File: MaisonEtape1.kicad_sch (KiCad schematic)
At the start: 6 parts, among them SW1 SW_DIP_x01, SW2 SW_DIP_x01, SW3 SW_DIP_x01, U1 ATmega328-P, U2 ATmega328-P

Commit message: Photon
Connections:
- net GND: now also Lt.22 (GND), Lt.8 (GND), U1.22 (GND), U1.8 (GND), U2.22 (GND), U2.8 (GND)
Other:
- added sheet Photon (Photon.kicad_sch)
- note added: "F1"
- note added: "F2"
- note added: "MASTER"
- note added: "Porte"
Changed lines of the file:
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@@
+    (stroke (width 0) (type default))
+  )
+  (wire (pts (xy 201.93 146.05) (xy 201.93 152.4))
     (stroke (width 0) (type default))
   )
@@
     (stroke (width 0) (type default))
   )
+  (wire (pts (xy 134.62 146.05) (xy 134.62 152.4))
+    (stroke (width 0) (type default))
+  )
   (wire (pts (xy 217.17 85.09) (xy 224.79 85.09))
     (stroke (width 0) (type default))
@@
   (wire (pts (xy 102.87 125.73) (xy 105.41 125.73))
     (stroke (width 0) (type default))
+  )
+  (wire (pts (xy 87.63 146.05) (xy 87.63 152.4))
+    (stroke (width 0) (type default))
+  )
+  (text "F2\n" (at 95.25 50.8 0)
+    (effects (font (size 2 2)) (justify left bottom))
+  )
+  (text "F1" (at 87.63 30.48 0)
+    (effects (font (size 2 2)) (justify left bottom))
+  )
+  (text "Porte" (at 130.81 30.48 0)
+    (effects (font (size 2 2)) (justify left bottom))
+  )
+  (text "MASTER" (at 204.47 147.32 0)
+    (effects (font (size 2 2)) (justify left bottom))
   )
   (global_label "i2c_SCL" (shape input) (at 110.49 113.03 0) (fields_autoplaced)
@@
     )
   )
+  (symbol (lib_id "power:GND") (at 134.62 152.4 0) (unit 1)
+    (in_bom yes) (on_board yes) (dnp no) (fields_autoplaced)
+    (property "Reference" "#PWR016" (at 134.62 158.75 0)
+      (effects (font (size 1.27 1.27)) hide)
+    )
+    (property "Value" "GND" (at 134.62 157.48 0)
+      (effects (font (size 1.27 1.27)))
+    )
+    (property "Footprint" "" (at 134.62 152.4 0)
+      (effects (font (size 1.27 1.27)) hide)
+    )
+    (property "Datasheet" "" (at 134.62 152.4 0)
+      (effects (font (size 1.27 1.27)) hide)
+    )
+    (pin "1")
+    (instances
+      (project "MaisonEtape1"
+        (path "/ed06f8de-d1bb-4b1a-bfe3-5df11d3a9162"
+          (reference "#PWR016") (unit 1)
+        )
+      )
+    )
+  )
+  (symbol (lib_id "power:GND") (at 87.63 152.4 0) (unit 1)
+    (in_bom yes) (on_board yes) (dnp no) (fields_autoplaced)
+    (property "Reference" "#PWR015" (at 87.63 158.75 0)
+      (effects (font (size 1.27 1.27)) hide)
+    )
+    (property "Value" "GND" (at 87.63 157.48 0)
+      (effects (font (size 1.27 1.27)))
+    )
+    (property "Footprint" "" (at 87.63 152.4 0)
+      (effects (font (size 1.27 1.27)) hide)
+    )
+    (property "Datasheet" "" (at 87.63 152.4 0)
+      (effects (font (size 1.27 1.27)) hide)
+    )
+    (pin "1")
+    (instances
+      (project "MaisonEtape1"
+        (path "/ed06f8de-d1bb-4b1a-bfe3-5df11d3a9162"
+          (reference "#PWR015") (unit 1)
+        )
+      )
+    )
+  )
   (symbol (lib_id "Switch:SW_DIP_x01") (at 133.35 39.37 0) (unit 1)
     (in_bom yes) (on_board yes) (dnp no) (fields_autoplaced)
@@
         (path "/ed06f8de-d1bb-4b1a-bfe3-5df11d3a9162"
           (reference "#PWR06") (unit 1)
+        )
+      )
+    )
+  )
+  (symbol (lib_id "power:GND") (at 201.93 152.4 0) (unit 1)
+    (in_bom yes) (on_board yes) (dnp no) (fields_autoplaced)
+    (property "Reference" "#PWR017" (at 201.93 158.75 0)
+      (effects (font (size 1.27 1.27)) hide)
+    )
+    (property "Value" "GND" (at 201.93 157.48 0)
+      (effects (font (size 1.27 1.27)))
+    )
+    (property "Footprint" "" (at 201.93 152.4 0)
+      (effects (font (size 1.27 1.27)) hide)
+    )
+    (property "Datasheet" "" (at 201.93 152.4 0)
+      (effects (font (size 1.27 1.27)) hide)
+    )
+    (pin "1")
+    (instances
+      (project "MaisonEtape1"
+        (path "/ed06f8de-d1bb-4b1a-bfe3-5df11d3a9162"
+          (reference "#PWR017") (unit 1)
         )
       )
@@
       )
     )
+  )
+  (sheet (at 308.61 67.31) (size 25.4 3.81) (fields_autoplaced)
+    (stroke (width 0.1524) (type solid))
+    (fill (color 0 0 0 0.0000))
+    (property "Sheetname" "Photon" (at 308.61 66.5984 0)
+      (effects (font (size 1.27 1.27)) (justify left bottom))
+    )
+    (property "Sheetfile" "Photon.kicad_sch" (at 308.61 71.7046 0)
+      (effects (font (size 1.27 1.27)) (justify left top))
+    )
+    (instances
+      (project "MaisonEtape1"
+        (path "/ed06f8de-d1bb-4b1a-bfe3-5df11d3a9162" (page "3"))
+      )
+    )

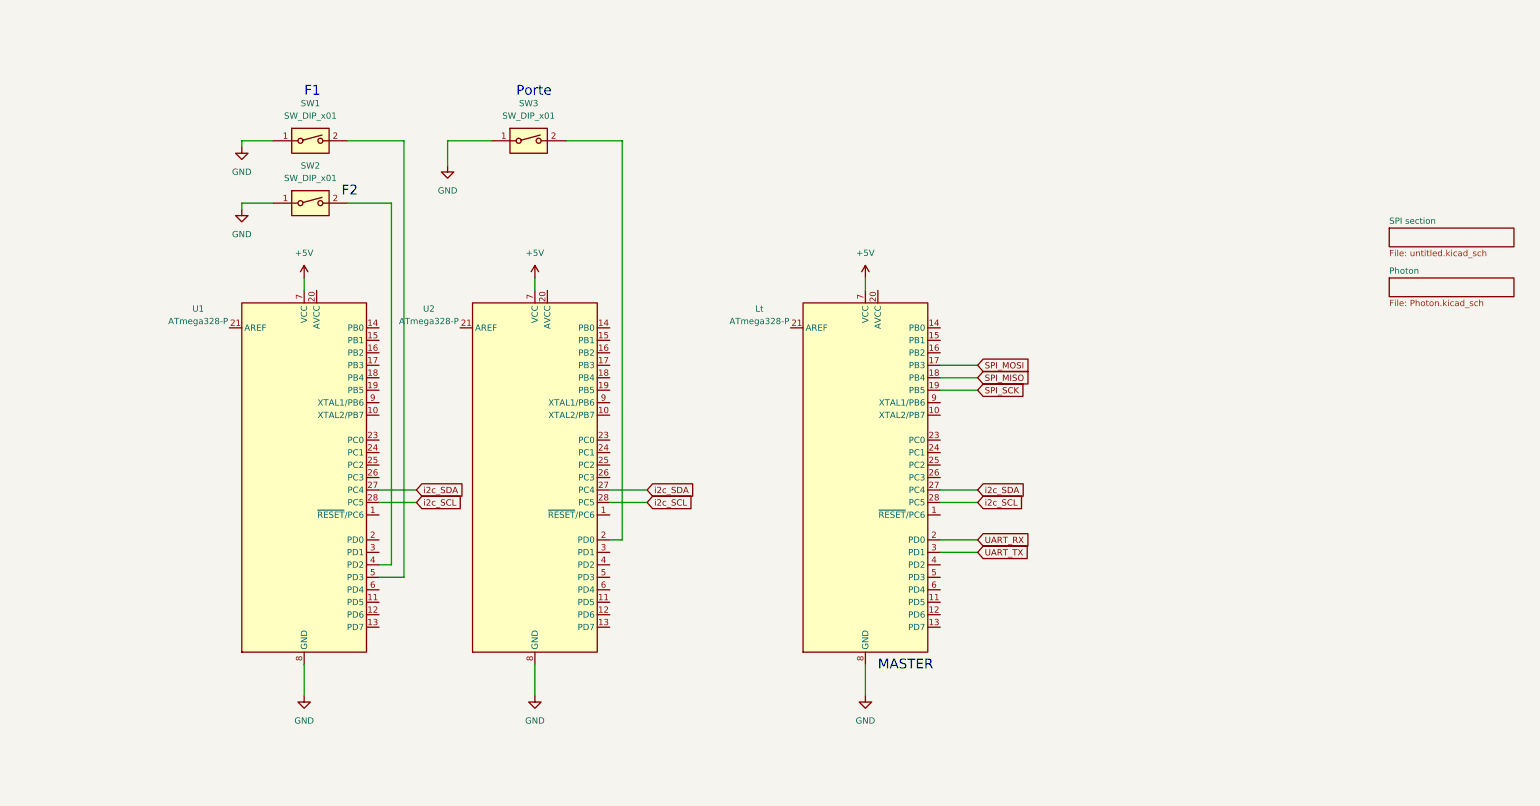
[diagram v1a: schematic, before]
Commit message: Connecteur AVR + Branchement MOSI/MISO/SCK + CS
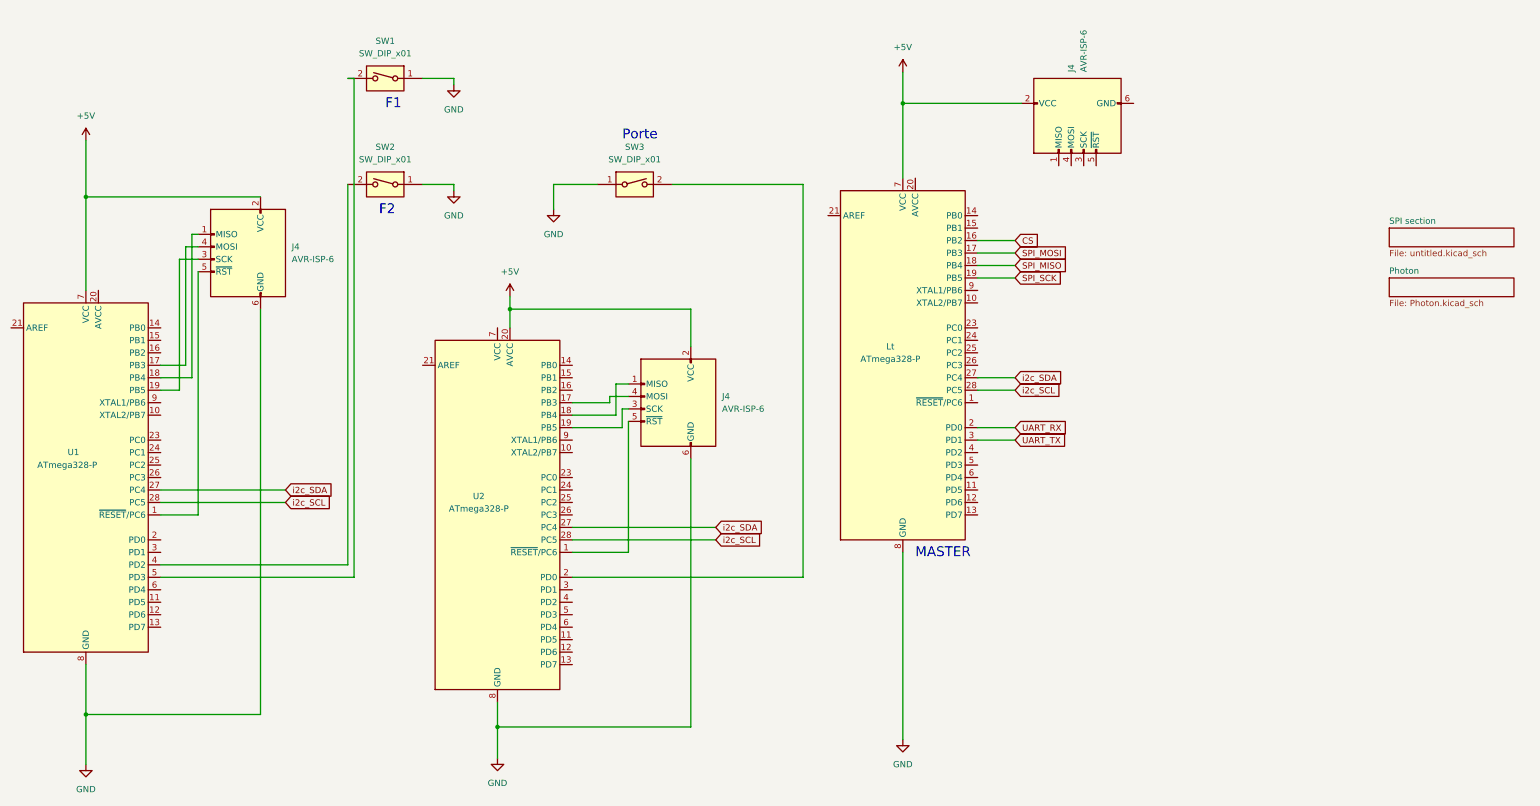
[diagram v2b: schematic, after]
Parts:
- added J4 (x3): AVR-ISP-6, Connector_IDC:IDC-Header_2x03_P2.54mm_Vertical, symbol Connector:AVR-ISP-6
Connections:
- net +5V: now also U2.20 (AVCC), J4.2 (VCC), J4.2 (VCC), J4.2 (VCC); no longer U2.7 (VCC)
- net GND: now also J4.6 (GND), J4.6 (GND)
- net CS: now reaches Lt.16 (PB2)
- net at U2.1 (~{RESET}/PC6): now also J4.5 (~{RST})
- net at U2.17 (PB3): now also J4.4 (MOSI)
- net at U2.18 (PB4): now also J4.1 (MISO)
- net at U2.19 (PB5): now also J4.3 (SCK)
- net at U1.1 (~{RESET}/PC6): now also J4.5 (~{RST})
- net at U1.17 (PB3): now also J4.4 (MOSI)
- net at U1.18 (PB4): now also J4.1 (MISO)
- net at U1.19 (PB5): now also J4.3 (SCK)
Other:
- moved on the sheet: Lt, SW1, SW2, SW3, U1, U2
